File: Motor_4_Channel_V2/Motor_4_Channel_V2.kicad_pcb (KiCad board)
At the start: 2 copper layers, 100 x 100 mm, 90 parts, among them J1 Conn_01x02_Male, J10 Conn_01x02_Male, J11 Conn_01x10_Male, J2 Conn_01x02_Male, J3 Conn_01x02_Male, J4 Conn_01x02_Male, J5 Conn_01x02_Male, J6 Conn_01x02_Male, J7 Conn_01x02_Male, J8 Conn_01x10_Male, J9 Conn_01x02_Male, K1 G8N-1L-DC12, K2 G8N-1L-DC12, K3 G8N-1L-DC12, K4 G8N-1L-DC12, P1 Pad, P10 Pad, P11 Pad, P12 Pad, P2 Pad, P3 Pad, P4 Pad, P5 Pad, P6 Pad, P7 Pad, P8 Pad, P9 Pad, Q1 Q_NMOS_GDS, Q2 Q_NMOS_GDS, Q3 Q_NMOS_GDS, Q4 Q_NMOS_GDS, Q5 Q_NMOS_GDS, Q6 Q_NMOS_GDS, Q7 Q_NMOS_GDS, Q8 Q_NMOS_GDS, SW1 SW_SPST, U1 SN74LVC1G139DCUR, U10 NC7WZ14P6XCT-ND, U11 MSP430G2553_LP, U12 G8NW-2H-DC12, U13 G8NW-2H-DC12, U14 G8NW-2H-DC12, U15 G8NW-2H-DC12, U2 SN74LVC1G139DCUR, U3 UA78M05IDCY, U4 UA78M33QDCYRG4Q1, U5 NC7WZ14P6XCT-ND, U6 NC7WZ14P6XCT-ND, U7 SN74LVC1G139DCUR, U8 SN74LVC1G139DCUR, U9 NC7WZ14P6XCT-ND

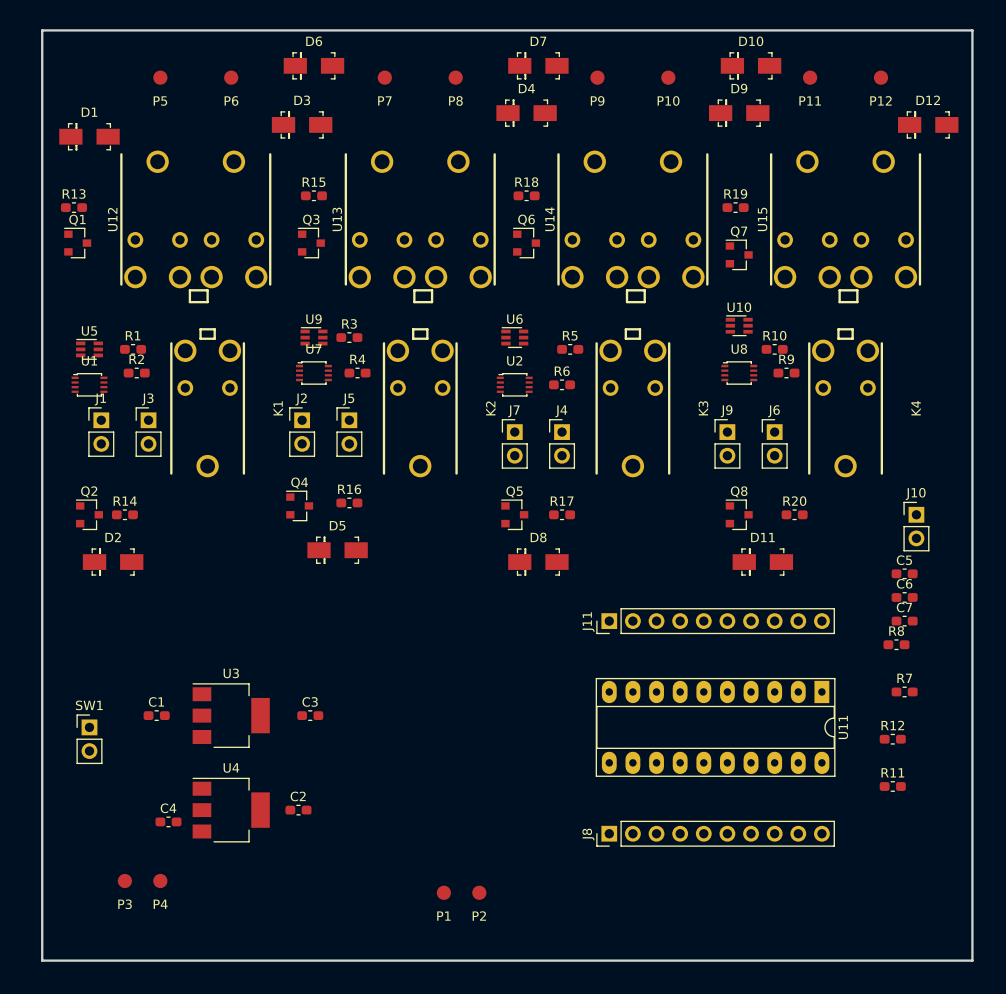
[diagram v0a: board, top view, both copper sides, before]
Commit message: Added progress to Motor 4 CH V2 layout.
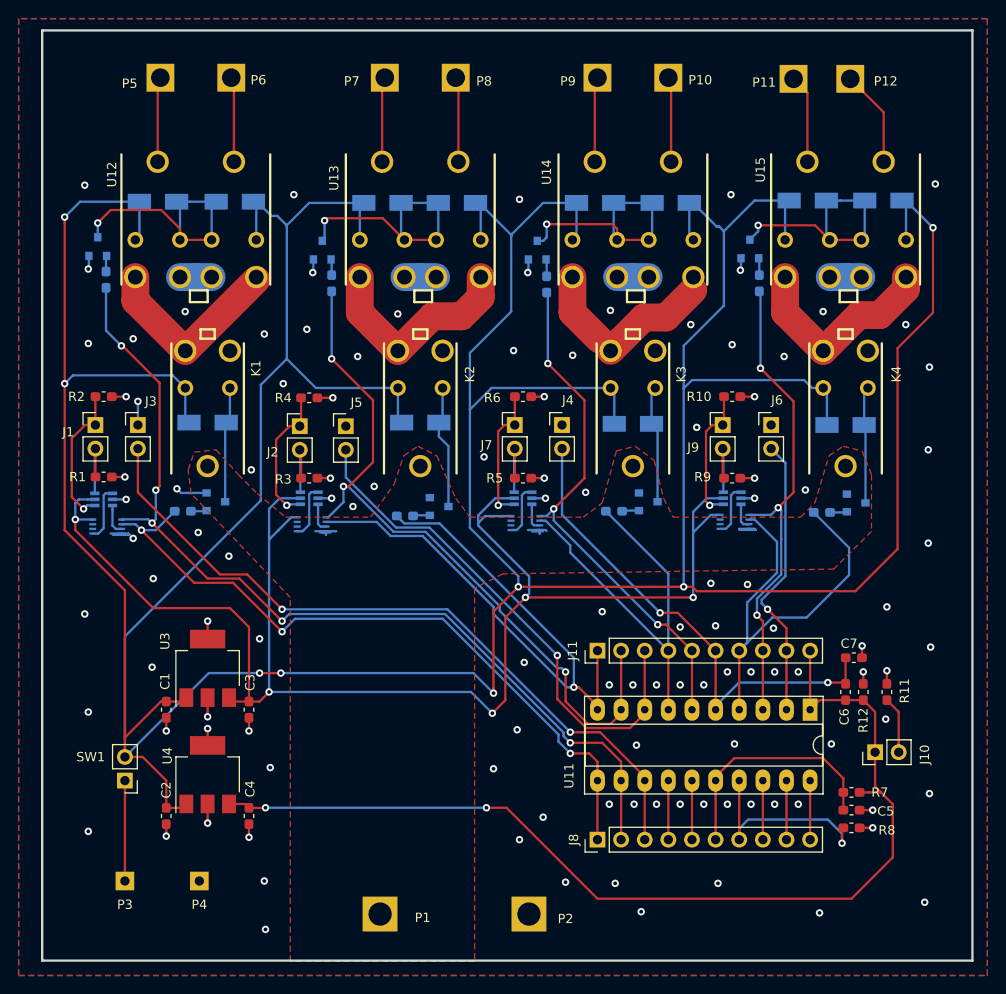
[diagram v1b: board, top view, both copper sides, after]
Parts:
- D1, D10, D11, D12, D2, D3, D4, D5, D6, D7, D8, D9, Q1, Q2, Q3, Q4, Q5, Q6, Q7, Q8, R13, R14, R15, R16, R17, R18, R19, R20, U1, U10, U2, U5, U6, U7, U8, U9: moved to B.Cu
- moved C5 26.0 mm to (177.2, 134.6)
- moved J10 25.9 mm to (179.7, 128.4), turned to 90 degrees
- moved R8 20.3 mm to (177.2, 136.5)
- moved U10 18.6 mm to (164.3, 101.1), turned to 180 degrees
- moved D2 18.1 mm to (108.0, 93.0)
- moved D8 18.0 mm to (153.7, 93.1)
- moved U6 17.3 mm to (141.9, 101.1), turned to 180 degrees
- moved U9 17.3 mm to (118.9, 101.1), turned to 180 degrees
- moved D11 17.2 mm to (176.5, 93.2)
- moved D6 16.5 mm to (126.7, 69.3)
- moved D5 16.3 mm to (130.8, 93.0)
- moved U7 16.3 mm to (119.1, 103.9), turned to 180 degrees
- moved U5 16.2 mm to (96.8, 101.2), turned to 180 degrees
- moved U8 16.0 mm to (164.6, 103.6), turned to 180 degrees
- moved D7 15.9 mm to (149.6, 69.3)
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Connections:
- C7 pad 1: DIR_3 -> BTN_3
- J1 pad 1: GREEN_4 -> GREEN_1
- J1 pad 2: RED_4 -> RED_1
- J11 pad 1: OUT_1 -> OUT_2
- J11 pad 2: DIR_1 -> DIR_2
- J11 pad 3: OUT_2 -> BTN_2
- J11 pad 4: DIR_2 -> OUT_3
- J11 pad 5: OUT_3 -> DIR_3
- J11 pad 6: DIR_3 -> BTN_3
- J11 pad 9: Net-(J11-Pad9) -> BTN_4
- J2 pad 1: GREEN_4 -> GREEN_2
- J2 pad 2: RED_4 -> RED_2
- J7 pad 1: GREEN_4 -> GREEN_3
- J7 pad 2: RED_4 -> RED_3
- J8 pad 1: BTN_4 -> OUT_1
- J8 pad 2: BTN_3 -> DIR_1
- J8 pad 3: BTN_2 -> BTN_1
- J8 pad 4: BTN_1 -> Net-(J8-Pad4)
- K1 pad 5: (no net) -> SW1_CTL
- K2 pad 5: (no net) -> SW2_CTL
- K3 pad 5: (no net) -> SW3_CTL
- K4 pad 5: (no net) -> SW4_CTL
- P2 pad 1: GND -> Net-(P2-Pad1)
- Q1 pad 2: M1_1B -> GND
- Q1 pad 3: GND -> M1_1B
- Q2 pad 2: SW1_CTL -> GND
- Q2 pad 3: GND -> SW1_CTL
- Q3 pad 2: M2_1B -> GND
- Q3 pad 3: GND -> M2_1B
- Q4 pad 2: SW2_CTL -> GND
- Q4 pad 3: GND -> SW2_CTL
- Q5 pad 2: SW3_CTL -> GND
- Q5 pad 3: GND -> SW3_CTL
- Q6 pad 2: M3_1B -> GND
- Q6 pad 3: GND -> M3_1B
- Q7 pad 2: M4_1B -> GND
- Q7 pad 3: GND -> M4_1B
- Q8 pad 2: SW4_CTL -> GND
- Q8 pad 3: GND -> SW4_CTL
- R1 pad 1: RED_4 -> RED_1
- R12 pad 1: DIR_3 -> BTN_3
- R2 pad 1: GREEN_4 -> GREEN_1
- R3 pad 1: RED_4 -> RED_2
- R4 pad 1: GREEN_4 -> GREEN_2
- R5 pad 1: RED_4 -> RED_3
- R6 pad 1: GREEN_4 -> GREEN_3
- U11 pad 10: OUT_1 -> OUT_2
- U11 pad 11: BTN_4 -> OUT_1
- U11 pad 12: BTN_3 -> DIR_1
- U11 pad 13: BTN_2 -> BTN_1
- U11 pad 14: BTN_1 -> Net-(J8-Pad4)
- U11 pad 2: Net-(J11-Pad9) -> BTN_4
- U11 pad 5: DIR_3 -> BTN_3
- U11 pad 6: OUT_3 -> DIR_3
- U11 pad 7: DIR_2 -> OUT_3
- U11 pad 8: OUT_2 -> BTN_2
- U11 pad 9: DIR_1 -> DIR_2
- U12 pad 4: GND -> Net-(U12-Pad4)
- U12 pad 8: GND -> Net-(U12-Pad4)
- U13 pad 4: GND -> Net-(U13-Pad4)
- U13 pad 8: GND -> Net-(U13-Pad4)
- U14 pad 4: GND -> Net-(U14-Pad4)
- U14 pad 8: GND -> Net-(U14-Pad4)
- U15 pad 4: GND -> Net-(U15-Pad4)
- U15 pad 8: GND -> Net-(U15-Pad4)
- U3 pad 1: GND -> 12V_REF
- U3 pad 2: 5V_REF -> GND
- U3 pad 3: 12V_REF -> 5V_REF
- U4 pad 1: GND -> 12V_REF
- U4 pad 2: 3V3_REF -> GND
- U4 pad 3: 12V_REF -> 3V3_REF
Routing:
- net 12V_REF: track 0.00 -> 525.9 mm, vias 0 -> 8
- net 5V_REF: track 0.00 -> 163.8 mm, vias 0 -> 5
- net 3V3_REF: track 0.00 -> 110.4 mm, vias 0 -> 2
- net DIR_1: track 0.00 -> 102.2 mm, vias 0 -> 5
- net BTN_1: track 0.00 -> 79.0 mm, vias 0 -> 2
- net DIR_2: track 0.00 -> 78.5 mm, vias 0 -> 3
- net OUT_1: track 0.00 -> 76.5 mm, vias 0 -> 3
- net OUT_2: track 0.00 -> 73.1 mm, vias 0 -> 1
- net GND: track 0.00 -> 72.4 mm, vias 0 -> 115
- net BTN_2: track 0.00 -> 56.4 mm, vias 0 -> 1
- net DIR_3: track 0.00 -> 56.4 mm, vias 0 -> 3
- net BTN_3: track 0.00 -> 54.3 mm, vias 0 -> 2
- net DIR_4: track 0.00 -> 52.1 mm, vias 0 -> 3
- net OUT_4: track 0.00 -> 47.2 mm
- net OUT_3: track 0.00 -> 44.2 mm
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- added copper zone on B.Cu, net GND
- added copper zone on F.Cu, net GND
- added copper zone on F.Cu, net V+
